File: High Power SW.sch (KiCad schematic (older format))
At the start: 15 parts, among them CN1 Jumper_NC_Small, Q1 FDD9407_F085, U1 PS2801C-1-A

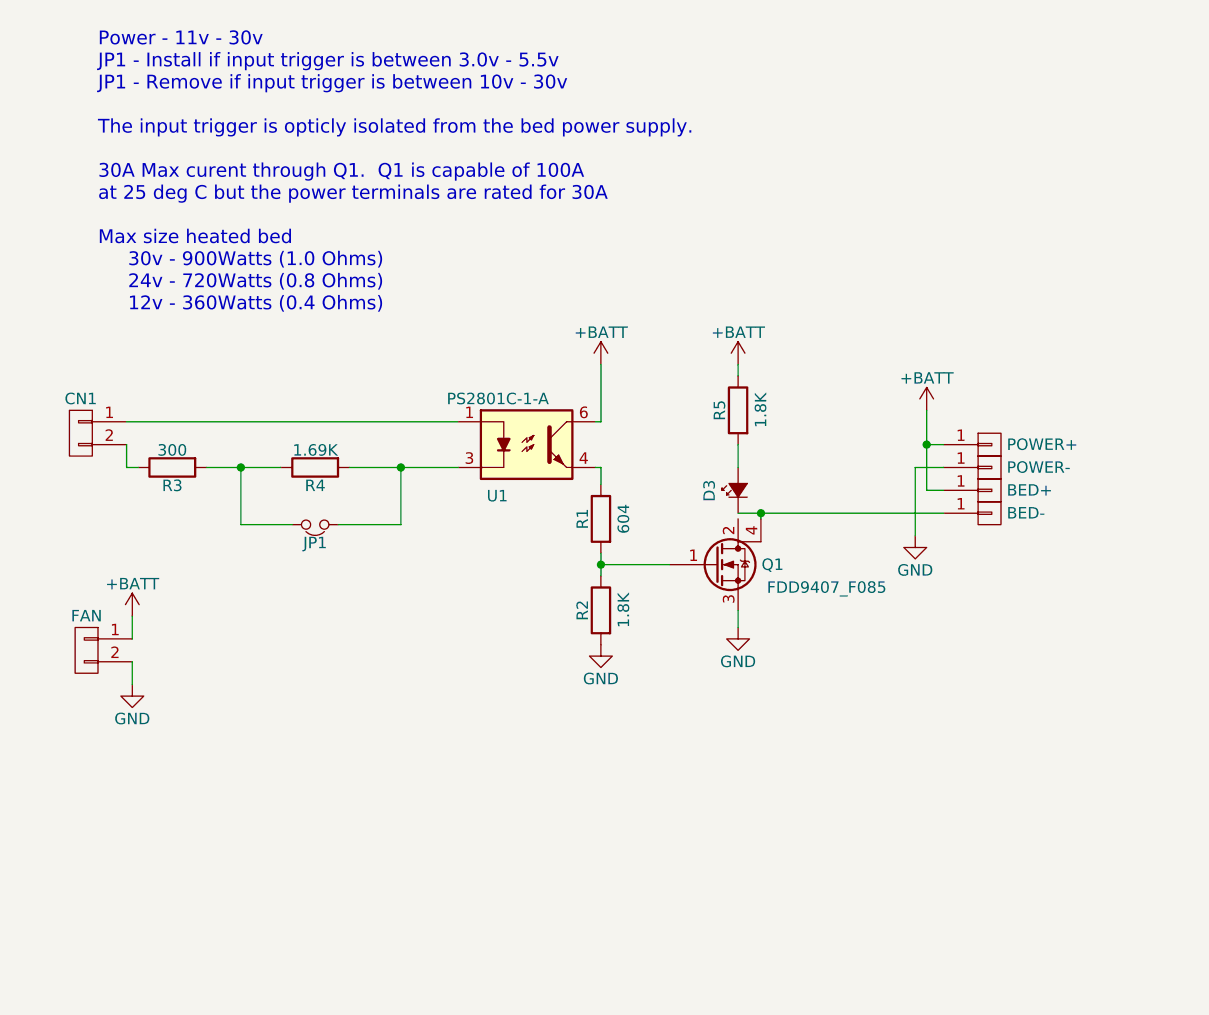
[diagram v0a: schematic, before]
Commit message: Update to schmatic and BOM
Updated R1 to 1.0K
Added mating connector information to schematic
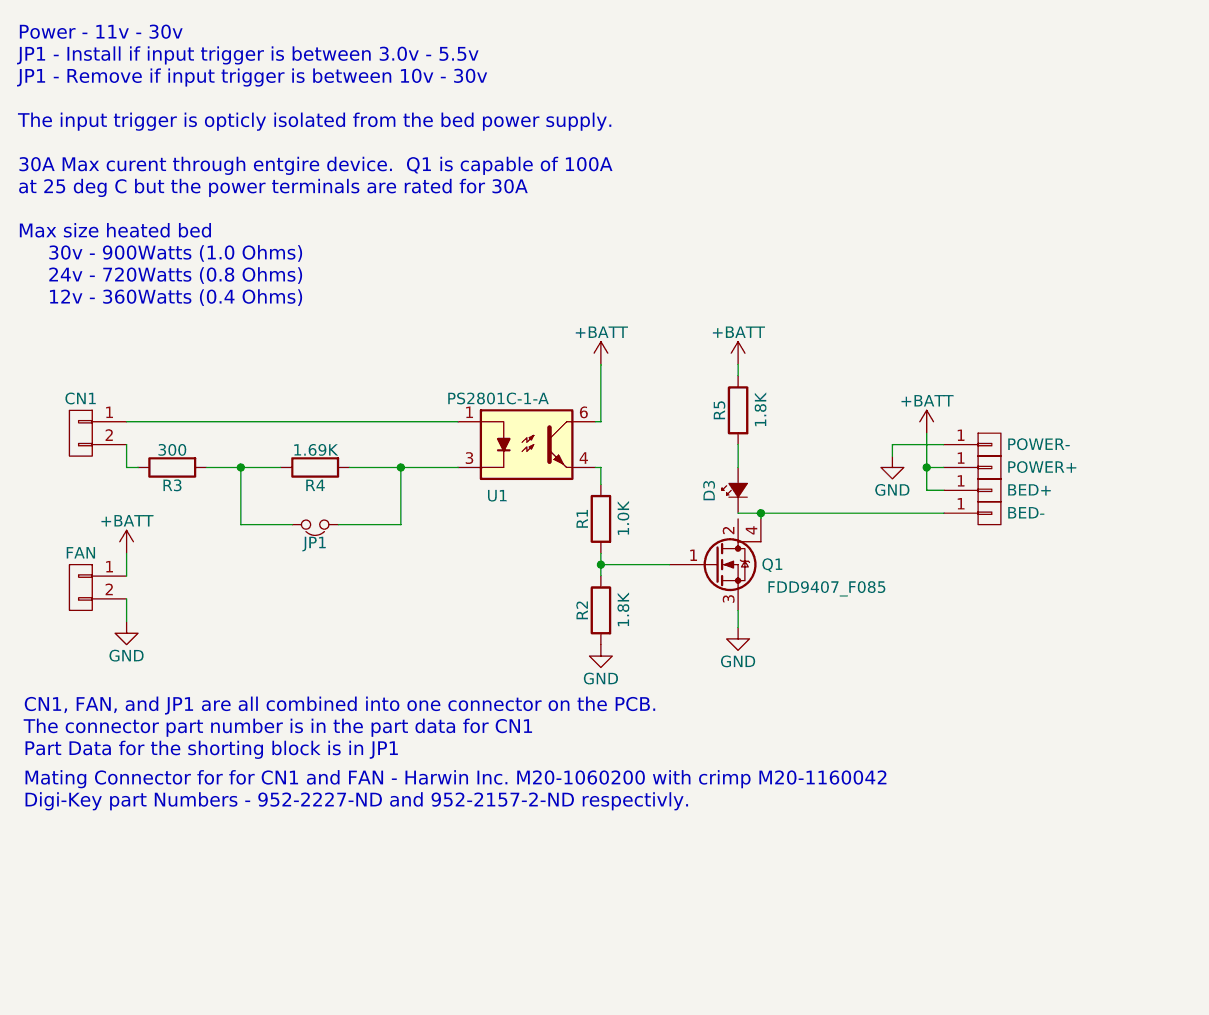
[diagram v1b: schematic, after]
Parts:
- FAN: footprint MyLib:10pin_connector -> (none); Manufacturer -NA- -> Harwin Inc.; Manufacturer_Part_No -NA- -> M20-1060200; Supplyer -NA- -> Digi-Key; Supplyer_Link -NA- -> http://www.digikey.com/product-detail/en/harwin-inc/M20-106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; Supplyer_Part_No -NA- -> 952-2227-ND
- R1: value 604 -> 1.0K; Manufacturer_Part_No RC1206FR-07604RL -> RC1206FR-071KL; Reel_Part_No 311-604FRTR-ND -> 311-1.00KFRTR-ND; Supplyer_Link http://www.digikey.com/product-detail/en/yageo/RC1206FR-072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 -> http://www.digikey.com/product-detail/en/yageo/RC1206FR-071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; Supplyer_Part_No 311-604FRCT-ND -> 311-1.00KFRCT-ND
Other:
- note added: "CN1, FAN, and JP1 are all combined into one connector on the PCB. \nThe connector part number is in the part data for CN1\nPart Data for the shorting block is in JP1\n"
- note added: "Mating Connector for for CN1 and FAN - Harwin Inc. M20-1060200 with crimp M20-1160042\nDigi-Key part Numbers - 952-2227-ND and 952-2157-2-ND respectivly."
- note added: "Power - 11v - 30v\nJP1 - Install if input trigger is between 3.0v - 5.5v\nJP1 - Remove if input trigger is between 10v - 30v\n\nThe input trigger is opticly isolated from the bed power supply.\n\n30A Max curent through entgire device. Q1 is capable of 100A \nat 25 deg C but the power terminals are rated for 30A\n\nMax size heated bed\n 30v - 900Watts (1.0 Ohms)\n 24v - 720Watts (0.8 Ohms)\n 12v -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"
- note removed: "Power - 11v - 30v\nJP1 - Install if input trigger is between 3.0v - 5.5v\nJP1 - Remove if input trigger is between 10v - 30v\n\nThe input trigger is opticly isolated from the bed power supply.\n\n30A Max curent through Q1. Q1 is capable of 100A \nat 25 deg C but the power terminals are rated for 30A\n\nMax size heated bed\n 30v - 900Watts (1.0 Ohms)\n 24v - 720Watts (0.8 Ohms)\n 12v - 360Watts (0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"
- moved on the sheet: FAN, POWER+, POWER-

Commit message: Bug Fix
Fixed Ki-Cad BOM generation error
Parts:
- FAN: footprint (none) -> MyLib:6pin_SMT_HEADER; Manufacturer Harwin Inc. -> -NA-; Manufacturer_Part_No M20-1060200 -> -NA-; Supplyer Digi-Key -> -NA-; Supplyer_Link http://www.digikey.com/product-detail/en/harwin-inc/M20-106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 -> -NA-; Supplyer_Part_No 952-2227-ND -> -NA-
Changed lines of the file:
@@
 F 0 "FAN" H 825 3175 50  0000 C CNN
 F 1 "Jumper_NC_Small" H 835 2965 50  0001 C CNN
-F 2 "" H 825 3025 50  0001 C CNN
-F 3 "https://cdn.harwin.com/pdfs/M20-106.pdf" H 825 3025 50  0001 C CNN
-F 4 "M20-1060200" H 825 3025 60  0001 C CNN "Manufacturer_Part_No"
-F 5 "Harwin Inc." H 825 3025 60  0001 C CNN "Manufacturer"
-F 6 "Digi-Key" H 825 3025 60  0001 C CNN "Supplyer"
-F 7 "http://www.digikey.com/product-detail/en/harwin-inc/M20-1060200/952-2227-ND/3728191" H 825 3025 60  0001 C CNN "Supplyer_Link"
-F 8 "952-2227-ND" H 825 3025 60  0001 C CNN "Supplyer_Part_No"
+F 2 "MyLib:6pin_SMT_HEADER" H 825 3025 50  0001 C CNN
+F 3 "-NA-" H 825 3025 50  0001 C CNN
+F 4 "-NA-" H 825 3025 60  0001 C CNN "Manufacturer_Part_No"
+F 5 "-NA-" H 825 3025 60  0001 C CNN "Manufacturer"
+F 6 "-NA-" H 825 3025 60  0001 C CNN "Supplyer"
+F 7 "-NA-" H 825 3025 60  0001 C CNN "Supplyer_Link"
+F 8 "-NA-" H 825 3025 60  0001 C CNN "Supplyer_Part_No"
 F 9 "-NA-" H 825 3025 60  0001 C CNN "Reel_Part_No"
 F 10 "-NA-" H 825 3025 60  0001 C CNN "Parts_Per_Reel"

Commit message: Added Logo's to the schmatic and pcb
Added a pending OSHWA Pending logo to the board
Added Digital Sqrt Logo to board
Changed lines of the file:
@@
 LIBS:contrib
 LIBS:valves
+LIBS:Logo-Digittle-Sqrt
 LIBS:High Power SW-cache
 EELAYER 25 0
@@
 Date "2016-11-26"
 Rev "1.5"
-Comp "Digital Sqrt"
+Comp ""
 Comment1 ""
 Comment2 ""
@@
 Wire Wire Line
 	4375 2400 4375 2450
+$Comp
+L LOGO #G?
+U 1 1 588038D4
+P 2325 4575
+F 0 "#G?" H 2325 4359 60  0001 C CNN
+F 1 "LOGO" H 2325 4791 60  0001 C CNN
+F 2 "" H 2325 4575 60  0001 C CNN
+F 3 "" H 2325 4575 60  0001 C CNN
+F 4 "Digi-Key" H 2325 4575 60  0001 C CNN "Supplyer"
+F 5 "Value" H 2325 4575 60  0001 C CNN "Parts_Per_Reel"
+	1    2325 4575
+	1    0    0    -1
+$EndComp
 $EndSCHEMATC

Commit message: Added CC ref
Little Driver is licensed under a
Creative Commons Attribution-ShareAlike 3.0 Unported License.
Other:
- note added: "Little Driver is licensed under a\nCreative Commons Attribution-ShareAlike 3.0 Unported License."
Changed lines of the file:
@@
 LIBS:valves
 LIBS:Logo-Digittle-Sqrt
+LIBS:CC-Logo
 LIBS:High Power SW-cache
 EELAYER 25 0
@@
 	1    0    0    -1
 $EndComp
+Text Notes 575  4225 0    60   ~ 0
+Little Driver is licensed under a\nCreative Commons Attribution-ShareAlike 3.0 Unported License.
 $EndSCHEMATC

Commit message: Update for KiCost
Updated Parts Lib so KiCost will work with KiCad
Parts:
- BED+, BED-, POWER+, POWER-: Manufacturer_Part_No 8197 -> (none); mfr_num (none) -> 8197
- CN1: Manufacturer_Part_No 95278-801A06LF -> (none); mfr_num (none) -> 95278-801A06LF
- D3: Manufacturer_Part_No CLM1B-AKW-CUAVB253 -> (none); mfr_num (none) -> CLM1B-AKW-CUAVB253
- FAN: Manufacturer_Part_No -NA- -> (none); mfr_num (none) -> -NA-
- JP1: Manufacturer_Part_No 969102-0000-DA -> (none); mfr_num (none) -> 969102-0000-DA
- Q1: Manufacturer_Part_No FDD9407_F085 -> (none); mfr_num (none) -> FDD9407_F085
- R1: Manufacturer_Part_No RC1206FR-071KL -> (none); mfr_num (none) -> RC1206FR-071KL
- R2, R5: Manufacturer_Part_No RC1206FR-071K8L -> (none); mfr_num (none) -> RC1206FR-071K8L
- R3: Manufacturer_Part_No RC1206JR-07300RL -> (none); mfr_num (none) -> RC1206JR-07300RL
- R4: Manufacturer_Part_No RC1206FR-071K69L -> (none); mfr_num (none) -> RC1206FR-071K69L
- U1: Manufacturer_Part_No PS2801C-1-A -> (none); mfr_num (none) -> PS2801C-1-A
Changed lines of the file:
@@
 F 2 "Resistors_SMD:R_1206_HandSoldering" V 1780 2500 50  0001 C CNN
 F 3 "http://www.yageo.com/NewPortal/yageodocoutput?fileName=/pdf/R-Chip/PYu-RC_Group_51_RoHS_L_4.pdf" H 1850 2500 50  0001 C CNN
-F 4 "RC1206FR-071K69L" H 1850 2500 60  0001 C CNN "Manufacturer_Part_No"
+F 4 "RC1206FR-071K69L" H 1850 2500 60  0001 C CNN "mfr_num"
 F 5 "Yageo" H 1850 2500 60  0001 C CNN "Manufacturer"
 F 6 "Digi-Key" H 1850 2500 60  0001 C CNN "Supplyer"
@@
 F 2 "MyLib:Keystone_terminal" H 4800 2500 50  0001 C CNN
 F 3 "http://www.keyelco.com/product-pdf.cfm?p=1534" H 4800 2500 50  0001 C CNN
-F 4 "8197" H 4800 2500 60  0001 C CNN "Manufacturer_Part_No"
+F 4 "8197" H 4800 2500 60  0001 C CNN "mfr_num"
 F 5 "Keystone Electronics" H 4800 2500 60  0001 C CNN "Manufacturer"
 F 6 "Digi-Key" H 4800 2500 60  0001 C CNN "Supplyer"
@@
 F 2 "MyLib:Keystone_terminal" H 4800 2600 50  0001 C CNN
 F 3 "http://www.keyelco.com/product-pdf.cfm?p=1534" H 4800 2600 50  0001 C CNN
-F 4 "8197" H 4800 2600 60  0001 C CNN "Manufacturer_Part_No"
+F 4 "8197" H 4800 2600 60  0001 C CNN "mfr_num"
 F 5 "Keystone Electronics" H 4800 2600 60  0001 C CNN "Manufacturer"
 F 6 "Digi-Key" H 4800 2600 60  0001 C CNN "Supplyer"
@@
 F 2 "MyLib:Keystone_terminal" H 4800 2700 50  0001 C CNN
 F 3 "http://www.keyelco.com/product-pdf.cfm?p=1534" H 4800 2700 50  0001 C CNN
-F 4 "8197" H 4800 2700 60  0001 C CNN "Manufacturer_Part_No"
+F 4 "8197" H 4800 2700 60  0001 C CNN "mfr_num"
 F 5 "Keystone Electronics" H 4800 2700 60  0001 C CNN "Manufacturer"
 F 6 "Digi-Key" H 4800 2700 60  0001 C CNN "Supplyer"
@@
 F 2 "Resistors_SMD:R_1206_HandSoldering" V 1155 2500 50  0001 C CNN
 F 3 "http://www.yageo.com/NewPortal/yageodocoutput?fileName=/pdf/R-Chip/PYu-RC_Group_51_RoHS_L_4.pdf" H 1225 2500 50  0001 C CNN
-F 4 "RC1206JR-07300RL" H 1225 2500 60  0001 C CNN "Manufacturer_Part_No"
+F 4 "RC1206JR-07300RL" H 1225 2500 60  0001 C CNN "mfr_num"
 F 5 "Yageo" H 1225 2500 60  0001 C CNN "Manufacturer"
 F 6 "Digi-Key" H 1225 2500 60  0001 C CNN "Supplyer"
@@
 F 2 "MyLib:SOP-4" H 2575 2200 50  0001 L CIN
 F 3 "http://www.digikey.com/product-search/en?keywords=PS2801C-1-A" H 2775 2400 50  0001 L CNN
-F 4 "PS2801C-1-A" H 2775 2400 60  0001 C CNN "Manufacturer_Part_No"
+F 4 "PS2801C-1-A" H 2775 2400 60  0001 C CNN "mfr_num"
 F 5 "CEL" H 2775 2400 60  0001 C CNN "Manufacturer"
 F 6 "Digi-Key" H 2775 2400 60  0001 C CNN "Supplyer"
@@
 F 2 "Resistors_SMD:R_1206_HandSoldering" V 3030 2725 50  0001 C CNN
 F 3 "http://www.yageo.com/NewPortal/yageodocoutput?fileName=/pdf/R-Chip/PYu-RC_Group_51_RoHS_L_4.pdf" H 3100 2725 50  0001 C CNN
-F 4 "RC1206FR-071KL" H 3100 2725 60  0001 C CNN "Manufacturer_Part_No"
+F 4 "RC1206FR-071KL" H 3100 2725 60  0001 C CNN "mfr_num"
 F 5 "Yageo" H 3100 2725 60  0001 C CNN "Manufacturer"
 F 6 "Digi-Key" H 3100 2725 60  0001 C CNN "Supplyer"
@@
 F 2 "MyLib:CREE_CLM1B_AKW_CUAVB253" V 3700 2600 50  0001 C CNN
 F 3 "http://www.cree.com/~/media/Files/Cree/LED%20Components%20and%20Modules/HB/Data%20Sheets/CLM1BRKWAKW1084.pdf" V 3700 2600 50  0001 C CNN
-F 4 "CLM1B-AKW-CUAVB253" H 3700 2600 60  0001 C CNN "Manufacturer_Part_No"
+F 4 "CLM1B-AKW-CUAVB253" H 3700 2600 60  0001 C CNN "mfr_num"
 F 5 "CREE" H 3700 2600 60  0001 C CNN "Manufacturer"
 F 6 "Digi-Key" H 3700 2600 60  0001 C CNN "Supplyer"
@@
 F 2 "MyLib:6pin_SMT_HEADER" H 825 2350 50  0001 C CNN
 F 3 "http://portal.fciconnect.com/Comergent//fci/drawing/95278.pdf" H 825 2350 50  0001 C CNN
-F 4 "95278-801A06LF" H 825 2350 60  0001 C CNN "Manufacturer_Part_No"
+F 4 "95278-801A06LF" H 825 2350 60  0001 C CNN "mfr_num"
 F 5 "Amphenol FCI" H 825 2350 60  0001 C CNN "Manufacturer"
 F 6 "Digi-Key" H 825 2350 60  0001 C CNN "Supplyer"
@@
 F 2 "MyLib:Cut_Jumper" H 1850 2750 50  0001 C CNN
 F 3 "http://multimedia.3m.com/mws/media/548120O/3mtm-shunt-ts2186.pdf" H 1850 2750 50  0001 C CNN
-F 4 "969102-0000-DA" H 1850 2750 60  0001 C CNN "Manufacturer_Part_No"
+F 4 "969102-0000-DA" H 1850 2750 60  0001 C CNN "mfr_num"
 F 5 "3M" H 1850 2750 60  0001 C CNN "Manufacturer"
 F 6 "Digi-Key" H 1850 2750 60  0001 C CNN "Supplyer"
@@
 F 2 "MyLib:6pin_SMT_HEADER" H 825 3025 50  0001 C CNN
 F 3 "-NA-" H 825 3025 50  0001 C CNN
-F 4 "-NA-" H 825 3025 60  0001 C CNN "Manufacturer_Part_No"
+F 4 "-NA-" H 825 3025 60  0001 C CNN "mfr_num"
 F 5 "-NA-" H 825 3025 60  0001 C CNN "Manufacturer"
 F 6 "-NA-" H 825 3025 60  0001 C CNN "Supplyer"
@@
 F 2 "Resistors_SMD:R_1206_HandSoldering" V 3030 3125 50  0001 C CNN
 F 3 "http://www.yageo.com/NewPortal/yageodocoutput?fileName=/pdf/R-Chip/PYu-RC_Group_51_RoHS_L_4.pdf" H 3100 3125 50  0001 C CNN
-F 4 "RC1206FR-071K8L" H 3100 3125 60  0001 C CNN "Manufacturer_Part_No"
+F 4 "RC1206FR-071K8L" H 3100 3125 60  0001 C CNN "mfr_num"
 F 5 "Yageo" H 3100 3125 60  0001 C CNN "Manufacturer"
 F 6 "Digi-Key" H 3100 3125 60  0001 C CNN "Supplyer"
@@
 F 2 "TO_SOT_Packages_SMD:TO-263-3Lead" H 3800 3025 50  0001 C CNN
 F 3 "https://www.fairchildsemi.com/datasheets/FD/FDD9407_F085.pdf" H 3600 2925 50  0001 C CNN
-F 4 "FDD9407_F085" H 3600 2925 60  0001 C CNN "Manufacturer_Part_No"
+F 4 "FDD9407_F085" H 3600 2925 60  0001 C CNN "mfr_num"
 F 5 "Fairchild Semiconductor" H 3600 2925 60  0001 C CNN "Manufacturer"
 F 6 "Digi-Key" H 3600 2925 60  0001 C CNN "Supplyer"
@@
 F 2 "Resistors_SMD:R_1206_HandSoldering" V 3630 2250 50  0001 C CNN
 F 3 "http://www.yageo.com/NewPortal/yageodocoutput?fileName=/pdf/R-Chip/PYu-RC_Group_51_RoHS_L_4.pdf" H 3700 2250 50  0001 C CNN
-F 4 "RC1206FR-071K8L" H 3700 2250 60  0001 C CNN "Manufacturer_Part_No"
+F 4 "RC1206FR-071K8L" H 3700 2250 60  0001 C CNN "mfr_num"
 F 5 "Yageo" H 3700 2250 60  0001 C CNN "Manufacturer"
 F 6 "Digi-Key" H 3700 2250 60  0001 C CNN "Supplyer"
@@
 F 2 "MyLib:Keystone_terminal" H 4800 2400 50  0001 C CNN
 F 3 "http://www.keyelco.com/product-pdf.cfm?p=1534" H 4800 2400 50  0001 C CNN
-F 4 "8197" H 4800 2400 60  0001 C CNN "Manufacturer_Part_No"
+F 4 "8197" H 4800 2400 60  0001 C CNN "mfr_num"
 F 5 "Keystone Electronics" H 4800 2400 60  0001 C CNN "Manufacturer"
 F 6 "Digi-Key" H 4800 2400 60  0001 C CNN "Supplyer"
@@
 	4375 2400 4375 2450
 $Comp
-L LOGO #G?
+L LOGO #G1
 U 1 1 588038D4
 P 2325 4575
-F 0 "#G?" H 2325 4359 60  0001 C CNN
+F 0 "#G1" H 2325 4359 60  0001 C CNN
 F 1 "LOGO" H 2325 4791 60  0001 C CNN
 F 2 "" H 2325 4575 60  0001 C CNN
